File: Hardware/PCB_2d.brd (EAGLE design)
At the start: 46 x 35 mm, 105 parts, among them IC1 BQ25180YBGR, IC3 BMA421, IC4 DRV2605YZFR, IC9 RT6160AWSC_RT6160AWSC, J1 503480-2400, J2 TC2030-IDC, J4 KH-TYPE-C-16P, Q1 20V/4.2A/52mΩ/1.4W, Q3 SI1308EDL-T1-GE3, SW1 2025-10-22_07-23-44_LIBRARY_E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, SW2 2025-10-22_07-23-44_LIBRARY_E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, SW3 2025-10-22_07-23-44_LIBRARY_E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, U1 NRF52840_QF, U3 MAX17048G+T10, X1 32MHz

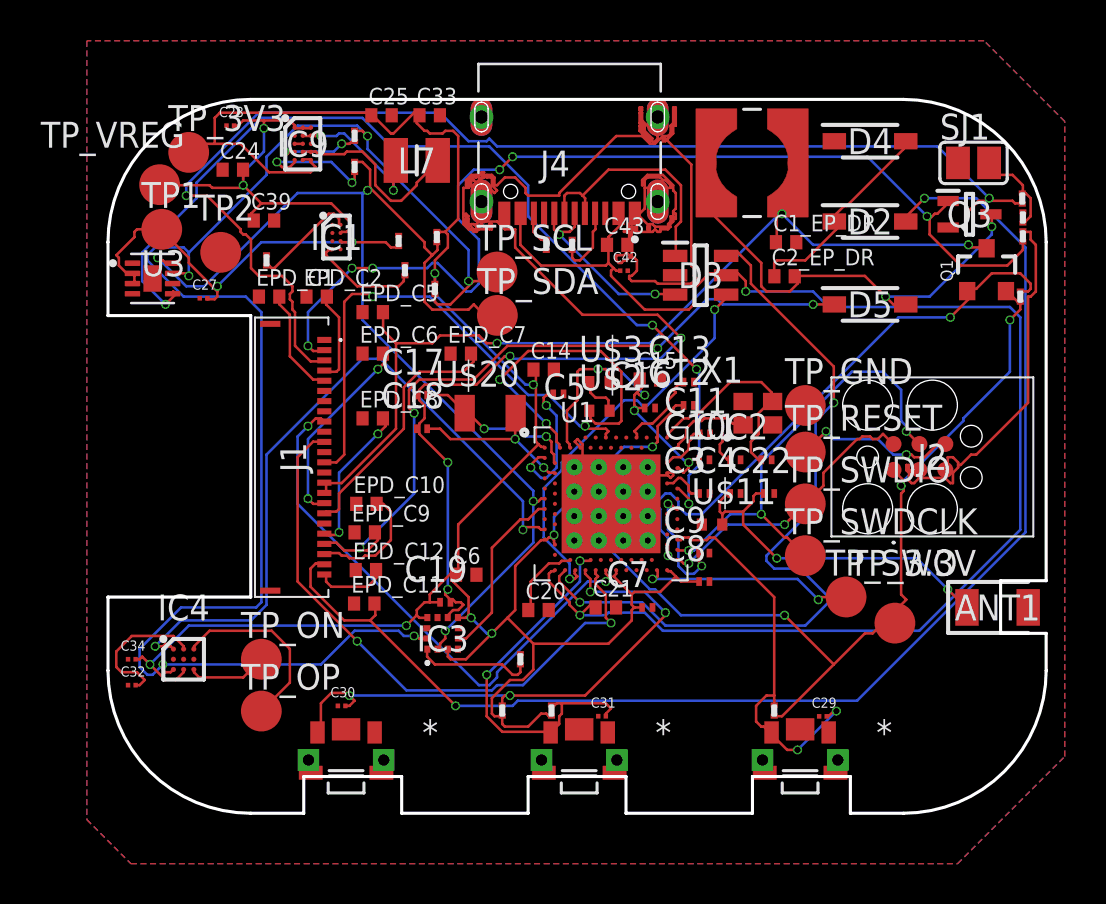
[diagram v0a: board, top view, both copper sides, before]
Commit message: Add modified files: Schematic, PCB_2d, PCB_3d in .f3d format(Fusion crashes at .step export), exploded_view in .f3z format(same problem), bill.bom, gerbers.zip, pick.cpl.
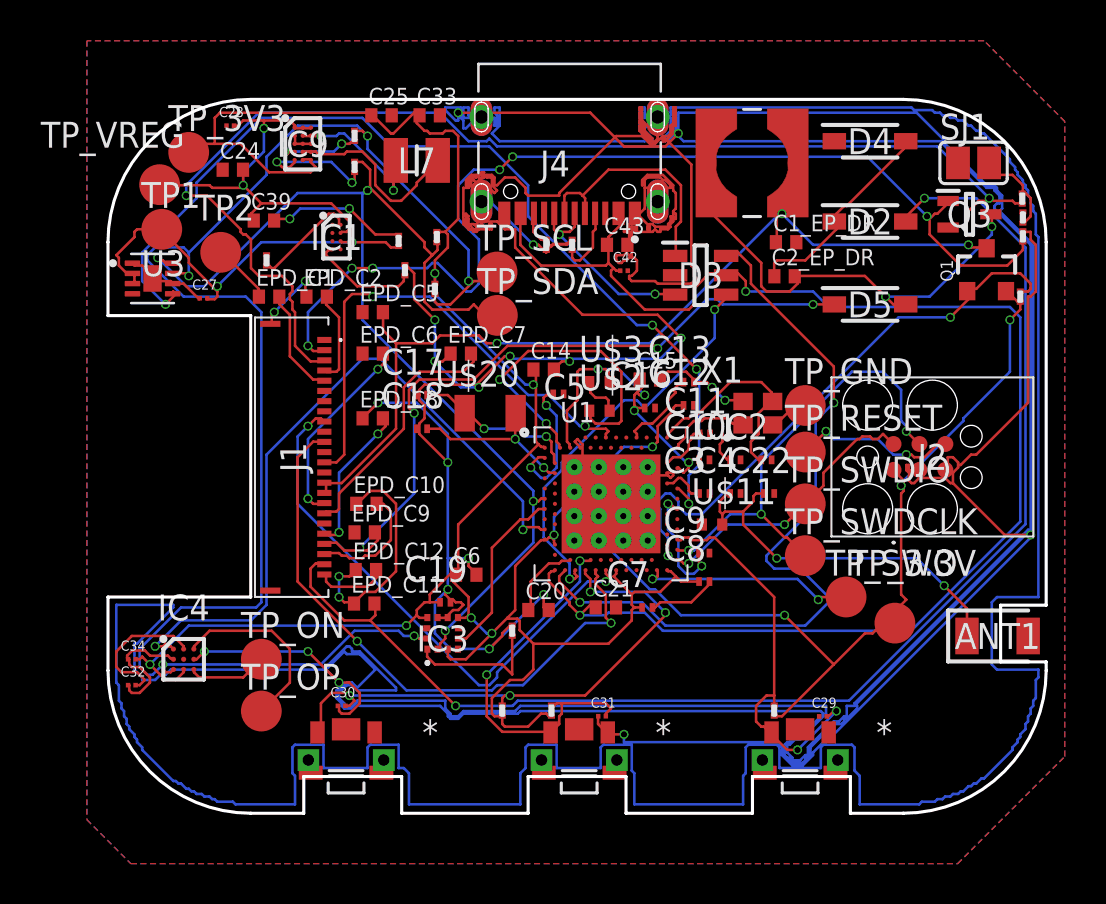
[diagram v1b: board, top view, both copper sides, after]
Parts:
- C10: value (none) -> N.C.
- C11: value (none) -> 100pF
- C25, C33: value (none) -> 22uF
- C43: value (none) -> 4.7uF
- moved R3 1.46 mm to (80.9, 45.9)
- moved ANT1 1.40 mm to (104.7, 45.6)
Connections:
- net N$59 renamed P0.01/XL2
- net N$75 renamed P0.00/XL1
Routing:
- net GND: track 140.1 -> 636.4 mm, vias 4 -> 28
- net N$25: track 17.8 -> 19.1 mm
- net N$80: track 5.72 -> 6.77 mm
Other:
- outline, holes or cut-outs redrawn
